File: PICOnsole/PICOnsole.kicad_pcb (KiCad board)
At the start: 2 copper layers, 22 parts, among them J1 UART Headers, SW1 A Button, SW2 X Button, SW3 Start Button, SW4 B Button, SW5 Y Button, SW6 DPad Right, SW7 DPad Down, SW8 DPad Up, SW9 DPad Left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

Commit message: Updated CAD files
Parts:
- added ?: , , F.Cu at (91.4, 101.6)
- added G***: LOGO, PICOnsole:QRCode_Soldermask, F.Cu at (90.7, 51.6)
- added J2: Vibration Motor, Connector_PinHeader_2.54mm:PinHeader_1x02_P2.54mm_Vertical, B.Cu at (77.3, 85.7)
- added J3: Amp Gain Jumper, Connector_PinHeader_2.54mm:PinHeader_1x05_P2.54mm_Vertical, B.Cu at (60.9, 98.4)
- added J4: Amp Gain Jumper2, Connector_PinHeader_2.54mm:PinHeader_1x05_P2.54mm_Vertical, B.Cu at (60.9, 100.9)
- added R1: 100K, Resistor_SMD:R_0805_2012Metric_Pad1.20x1.40mm_HandSolder, B.Cu at (59.8, 94.4)
- added R2: 100K, Resistor_SMD:R_0805_2012Metric_Pad1.20x1.40mm_HandSolder, B.Cu at (51.9, 94.4)
- added R3: 10K, Resistor_SMD:R_0805_2012Metric_Pad1.20x1.40mm_HandSolder, F.Cu at (79.5, 53.3)
- added R4: 1K, Resistor_SMD:R_0805_2012Metric_Pad1.20x1.40mm_HandSolder, F.Cu at (75.1, 53.3)
- added REF**: MountingHole_2.5mm_Pad, MountingHole:MountingHole_2.5mm_Pad, F.Cu at (88.9, 17.8)
- added REF**: MountingHole_2.5mm_Pad, MountingHole:MountingHole_2.5mm_Pad, F.Cu at (17.8, 101.6)
- added REF**: MountingHole_2.5mm_Pad, MountingHole:MountingHole_2.5mm_Pad, F.Cu at (17.8, 17.8)
- added SW10: Power Switch, Connector_PinHeader_2.54mm:PinHeader_1x03_P2.54mm_Vertical, F.Cu at (76.0, 15.2)
- added U4: Battery Charging Module, Connector_PinHeader_2.54mm:PinHeader_1x05_P2.54mm_Vertical, F.Cu at (94.5, 20.3)
- added U5: I2S Amp, Connector_PinHeader_2.54mm:PinHeader_1x07_P2.54mm_Vertical, B.Cu at (81.1, 48.8)
- J1, U3: moved to F.Cu
- moved D4 183.7 mm to (43.0, 25.4), turned to 0 degrees
- moved D5 177.9 mm to (43.0, 29.2), turned to 0 degrees
- moved D6 172.1 mm to (43.0, 33.0), turned to 0 degrees
- moved D2 170.5 mm to (40.5, 29.2), turned to 180 degrees
- moved D3 164.7 mm to (40.5, 33.0), turned to 180 degrees
- moved D9 163.1 mm to (29.1, 48.2), turned to 180 degrees
- moved D1 161.7 mm to (40.5, 25.4), turned to 180 degrees
- moved D7 157.5 mm to (29.1, 52.0), turned to 180 degrees
- moved SW2 147.2 mm to (67.2, 77.6), turned to -90 degrees
- moved D8 142.8 mm to (38.0, 60.9), turned to 180 degrees
- moved SW1 131.9 mm to (71.2, 94.0)
- moved SW4 131.9 mm to (87.6, 90.1)
- moved SW3 130.3 mm to (52.6, 60.0)
- moved SW7 129.4 mm to (28.0, 94.0)
- moved SW8 129.4 mm to (40.5, 73.6)
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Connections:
- U1 pad 19: unconnected-(U1-Pad19) -> /I2S_CLK
- U1 pad 20: unconnected-(U1-Pad20) -> /I2S_LRC
- U1 pad 24: /Input Cathode 3 -> /Input Anode 3
- U1 pad 27: /Input Anode 3 -> /Input Cathode 3
- U1 pad 29: unconnected-(U1-Pad29) -> /I2S_DIN
- U1 pad 36: unconnected-(U1-Pad36) -> +3V3
- U1 pad 39: +3V3 -> VSS
- U1 pad 9: unconnected-(U1-Pad9) -> /Motor
- U2 pad 39: +3V3 -> VSS
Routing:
- net Net-(D1-Pad2): track 53.6 -> 135.0 mm
- net /Input Anode 2: track 90.4 -> 12.7 mm
- net /Input Anode 1: track 89.9 -> 14.0 mm
- net /I2S_Gain: track 0.00 -> 74.0 mm
- net Net-(D2-Pad2): track 20.4 -> 85.5 mm
- net +3V3: track 91.4 -> 156.4 mm, vias 0 -> 1
- net Net-(D4-Pad2): track 26.8 -> 88.5 mm
- net /Input Anode 3: track 109.6 -> 48.0 mm
- net /I2S_CLK: track 0.00 -> 58.3 mm
- net /I2S_LRC: track 0.00 -> 58.0 mm
- net /Motor: track 0.00 -> 53.0 mm
- net Net-(D3-Pad2): track 19.6 -> 59.3 mm
- net /I2S_DIN: track 0.00 -> 37.0 mm
- net /BAT_GND: track 0.00 -> 23.7 mm
- net GND: track 22.4 -> 0.00 mm
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- added copper zone on B.Cu, net GND
- added copper zone on F.Cu, net GND
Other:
- board outline added: 83.8 x 94 mm
- board text added: "JLCJLCJLCJLC"
- board text added: "PICOnsole V1 By Bryce Dixon"

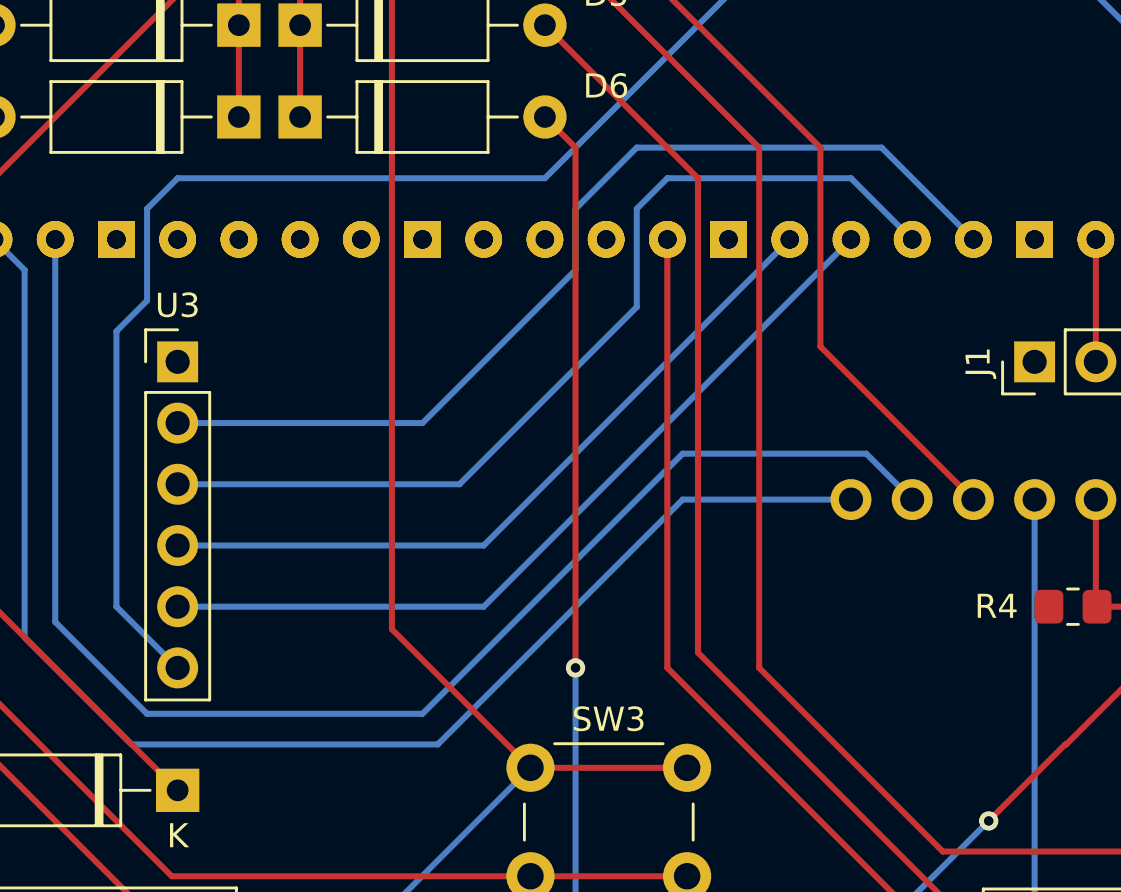
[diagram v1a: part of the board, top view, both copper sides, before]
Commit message: Increased OS RAM size to allow for better errors. Currently programs can't find builtin functions (eg memset) correctly
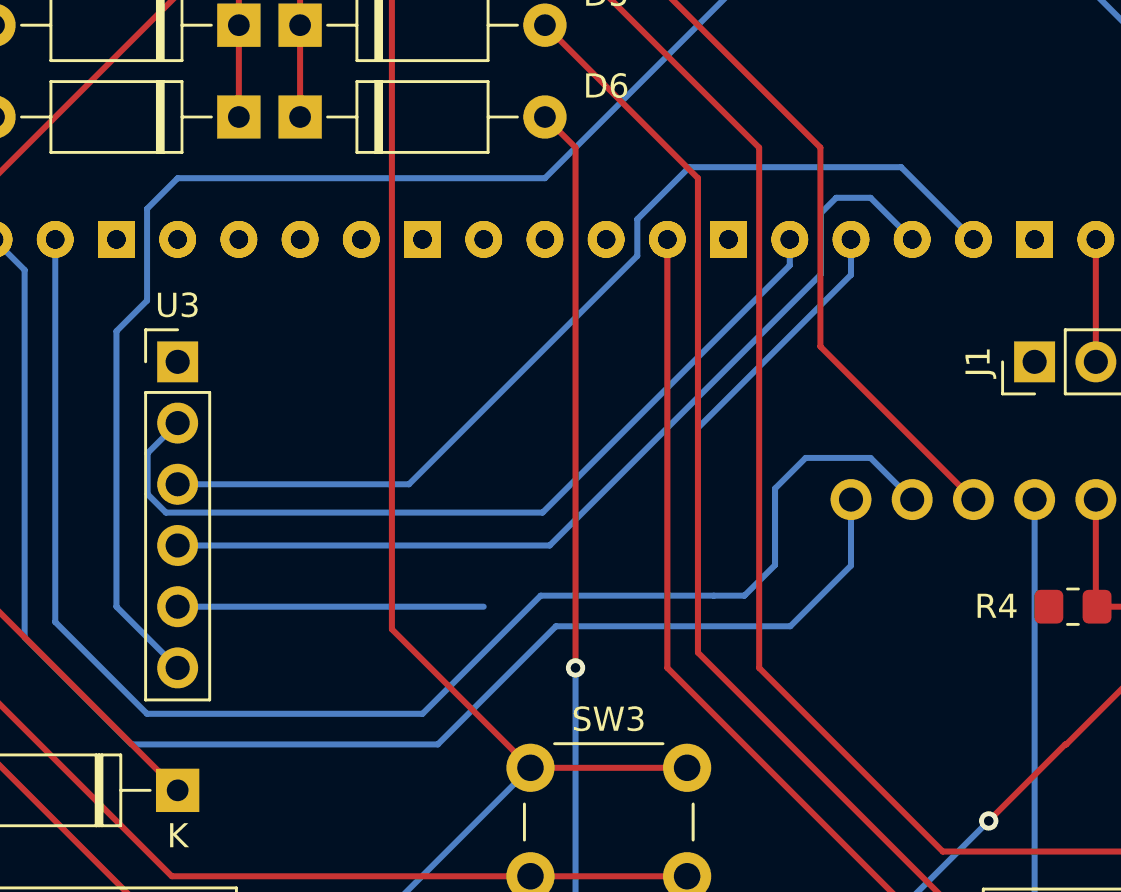
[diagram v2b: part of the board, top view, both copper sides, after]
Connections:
- net /I2S_SD renamed /0.3V
- U2 pad 1: unconnected-(U2-Pad1) -> /UART TX
- U2 pad 2: unconnected-(U2-Pad2) -> /UART RX
- U2 pad 21: unconnected-(U2-Pad21) -> /Input Cathode 1
- U2 pad 22: unconnected-(U2-Pad22) -> /Input Cathode 2
- U2 pad 24: unconnected-(U2-Pad24) -> /Input Anode 3
- U2 pad 25: unconnected-(U2-Pad25) -> /Input Anode 1
- U2 pad 26: unconnected-(U2-Pad26) -> /Input Anode 2
- U2 pad 27: unconnected-(U2-Pad27) -> /Input Cathode 3
- U2 pad 29: unconnected-(U2-Pad29) -> /I2S_DIN
- U2 pad 36: unconnected-(U2-Pad36) -> +3V3
- U2 pad 4: unconnected-(U2-Pad4) -> /SD CLK
- U2 pad 5: unconnected-(U2-Pad5) -> /SD MOSI
- U2 pad 6: unconnected-(U2-Pad6) -> /SD MISO
- U2 pad 7: unconnected-(U2-Pad7) -> /SD CS
- U2 pad 9: unconnected-(U2-Pad9) -> /Motor
- U3 pad 2: /SD CLK -> /SD MISO
- U3 pad 3: /SD MOSI -> /SD CLK
- U3 pad 4: /SD MISO -> /SD MOSI
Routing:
- net /SD CS: track 34.3 -> 23.1 mm
- net /SD MISO: track 30.7 -> 35.8 mm
- net /I2S_CLK: track 58.3 -> 60.0 mm
- net /I2S_LRC: track 58.0 -> 59.6 mm
- net /SD MOSI: track 39.2 -> 38.7 mm
